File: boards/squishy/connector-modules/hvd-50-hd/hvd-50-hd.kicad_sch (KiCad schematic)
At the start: 14 parts, among them J1 SCSI PHY Mezz, J3 Conn_01x04, J5 HD-50, U1 M24C02-RMC

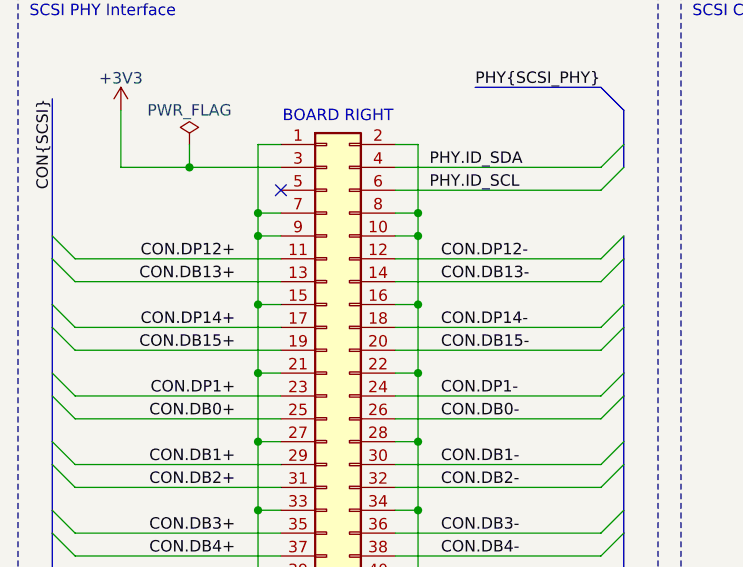
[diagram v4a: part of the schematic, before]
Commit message: squishy: connectors: s/DP12/DB12/g s/DP14/DB14/g
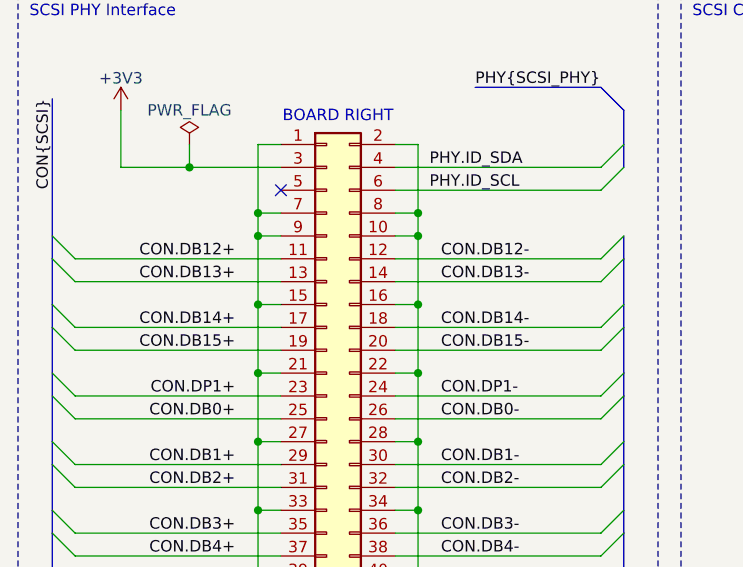
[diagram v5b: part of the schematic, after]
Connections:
- net CON.DP12+ renamed CON.DB12+
- net CON.DP12- renamed CON.DB12-
- net CON.DP14+ renamed CON.DB14+
- net CON.DP14- renamed CON.DB14-
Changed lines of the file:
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@@
 		)
 	)
-	(label "CON.DP14-"
+	(label "CON.DB14-"
 		(at 60.96 52.07 0)
 		(fields_autoplaced yes)
@@
 		)
 	)
-	(label "CON.DP12+"
+	(label "CON.DB12+"
 		(at 38.1 44.45 180)
 		(fields_autoplaced yes)
@@
 		)
 	)
-	(label "CON.DP12-"
+	(label "CON.DB12-"
 		(at 60.96 44.45 0)
 		(fields_autoplaced yes)
@@
 		)
 	)
-	(label "CON.DP14+"
+	(label "CON.DB14+"
 		(at 38.1 52.07 180)
 		(fields_autoplaced yes)

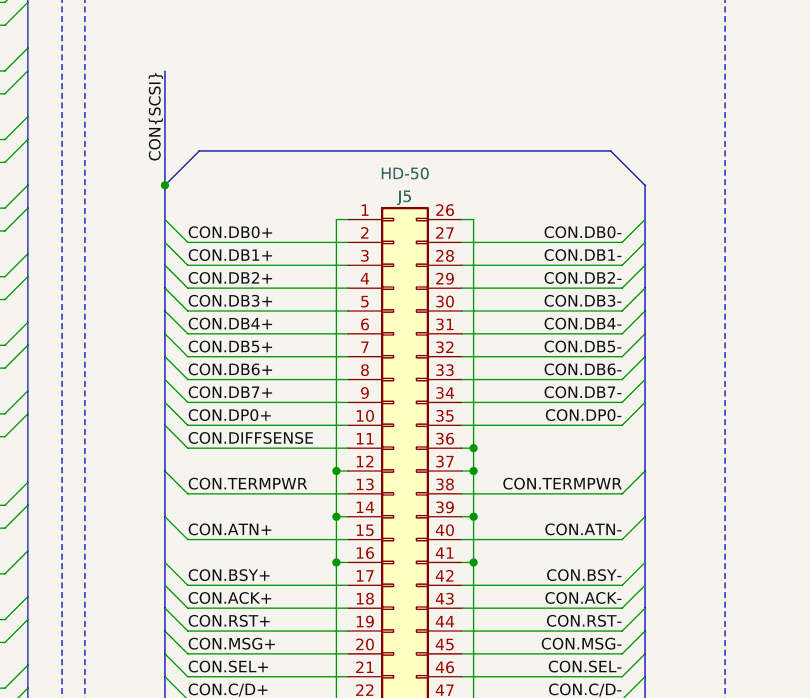
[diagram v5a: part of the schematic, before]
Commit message: squishy: connectors: updated SCSI connector metadata for hvd-50-hd
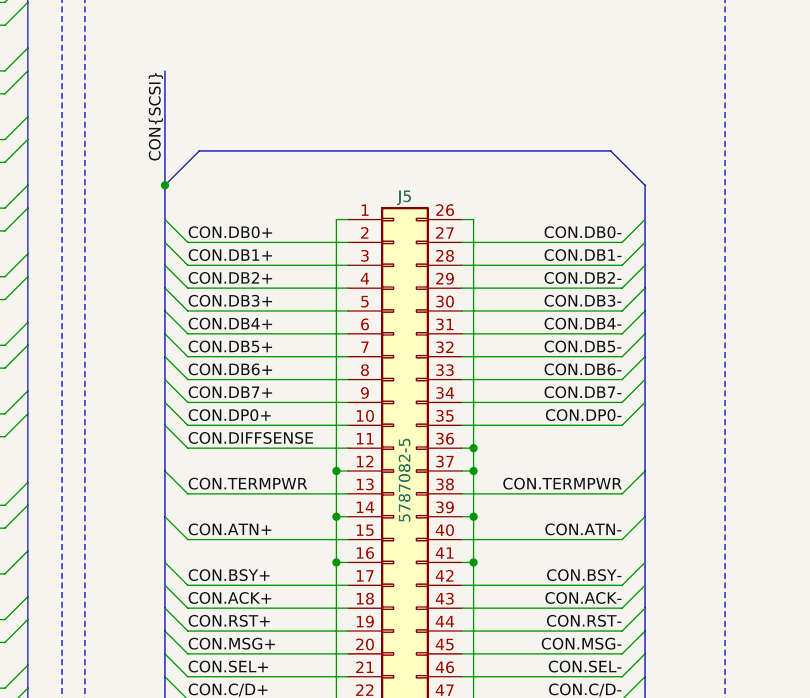
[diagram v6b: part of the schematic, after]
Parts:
- J5: value HD-50 -> 5787082-5; MFR (none) -> TE Connectivity; MPN (none) -> 5787082-5; URL (none) -> https://www.te.com/en/product-5787082-5.html
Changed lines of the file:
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@@
 			)
 		)
-		(property "Value" "HD-50"
-			(at 123.19 63.5 0)
+		(property "Value" "5787082-5"
+			(at 123.19 97.536 90)
 			(effects
 				(font
@@
 			)
 		)
-		(property "Datasheet" "~"
+		(property "Datasheet" "https://www.te.com/commerce/DocumentDelivery/DDEController?Action=showdoc&DocId=Specification+Or+Standard%7F114-40029%7FJ%7Fpdf%7FEnglish%7FENG_SS_114-40029_J.pdf%7F5787082-5"
 			(at 121.92 116.84 0)
 			(effects
@@
 			)
 		)
-		(property "Description" "Generic connector, double row, 02x25, counter clockwise pin numbering scheme (similar to DIP package numbering), with shielding"
+		(property "Description" "AMPLITE 1.27mm High-density D-subminiature 50-pin connector"
 			(at 123.19 97.79 0)
 			(effects
+				(font
+					(size 1.27 1.27)
+				)
+				(hide yes)
+			)
+		)
+		(property "MFR" "TE Connectivity"
+			(at 123.19 97.79 0)
+			(effects
+				(font
+					(size 1.27 1.27)
+				)
+				(hide yes)
+			)
+		)
+		(property "MPN" "5787082-5"
+			(at 123.19 97.79 0)
+			(effects
+				(font
+					(size 1.27 1.27)
+				)
+				(hide yes)
+			)
+		)
+		(property "URL" "https://www.te.com/en/product-5787082-5.html"
+			(at 123.19 97.79 0)
+			(effects

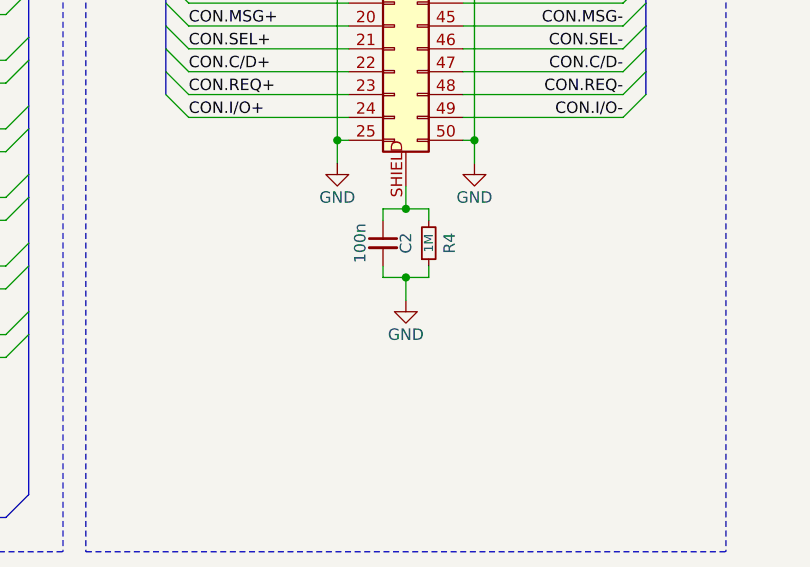
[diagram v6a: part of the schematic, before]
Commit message: squishy: connectors: Routed and length matched the hvd-50-hd connector interface
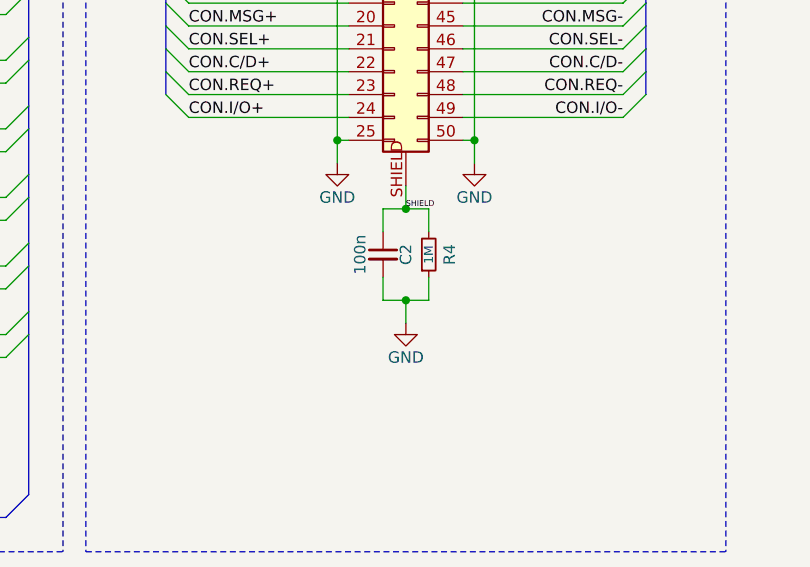
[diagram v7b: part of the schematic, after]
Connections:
- net SHIELD: now reaches C2.1, J5.SHIELD, R4.2
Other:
- moved on the sheet: C2, R4
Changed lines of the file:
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@@
 	)
 	(junction
-		(at 123.19 144.78)
+		(at 123.19 147.32)
 		(diameter 0)
 		(color 0 0 0 0)
@@
 	(wire
 		(pts
-			(xy 123.19 144.78) (xy 125.73 144.78)
+			(xy 123.19 147.32) (xy 125.73 147.32)
 		)
 		(stroke
@@
 	(wire
 		(pts
-			(xy 125.73 137.16) (xy 125.73 138.43)
+			(xy 125.73 137.16) (xy 125.73 139.7)
 		)
 		(stroke
@@
 	(wire
 		(pts
-			(xy 123.19 144.78) (xy 123.19 147.32)
+			(xy 123.19 147.32) (xy 123.19 149.86)
 		)
 		(stroke
@@
 	(wire
 		(pts
-			(xy 120.65 143.51) (xy 120.65 144.78)
+			(xy 120.65 144.78) (xy 120.65 147.32)
+		)
+		(stroke
+			(width 0)
+			(type default)
+		)
+	)
+	(wire
+		(pts
+			(xy 125.73 144.78) (xy 125.73 147.32)
 		)
 		(stroke
@@
 		)
 	)
-	(wire
-		(pts
-			(xy 125.73 143.51) (xy 125.73 144.78)
-		)
-		(stroke
-			(width 0)
-			(type default)
-		)
-	)
 	(bus
 		(pts
@@
 	(wire
 		(pts
-			(xy 120.65 137.16) (xy 120.65 138.43)
+			(xy 120.65 137.16) (xy 120.65 139.7)
 		)
 		(stroke
@@
 	(wire
 		(pts
-			(xy 120.65 144.78) (xy 123.19 144.78)
+			(xy 120.65 147.32) (xy 123.19 147.32)
 		)
 		(stroke
@@
 		)
 	)
+	(label "SHIELD"
+		(at 123.19 137.16 0)
+		(fields_autoplaced yes)
+		(effects
+			(font
+				(size 0.635 0.635)
+			)
+			(justify left bottom)
+		)
+	)
 	(label "CON.I{slash}O+"
 		(at 99.06 127 0)
@@
 	(symbol
 		(lib_id "power:GND")
-		(at 123.19 147.32 0)
+		(at 123.19 149.86 0)
 		(unit 1)
 		(exclude_from_sim no)
@@
 		(dnp no)
 		(property "Reference" "#PWR012"
-			(at 123.19 153.67 0)
+			(at 123.19 156.21 0)
 			(effects
 				(font
@@
 		)
 		(property "Value" "GND"
-			(at 123.19 151.13 0)
+			(at 123.19 153.67 0)
 			(effects
 				(font
@@
 		)
 		(property "Footprint" ""
-			(at 123.19 147.32 0)
+			(at 123.19 149.86 0)
 			(effects
 				(font
@@
 		)
 		(property "Datasheet" ""
-			(at 123.19 147.32 0)
+			(at 123.19 149.86 0)
 			(effects
 				(font
@@
 		)
 		(property "Description" "Power symbol creates a global label with name \"GND\" , ground"
-			(at 123.19 147.32 0)
+			(at 123.19 149.86 0)
 			(effects
 				(font
@@
 	(symbol
 		(lib_id "Device:R_Small")
-		(at 125.73 140.97 0)
+		(at 125.73 142.24 0)
 		(mirror x)
 		(unit 1)
@@
 		(dnp no)
 		(property "Reference" "R4"
-			(at 128.778 140.97 90)
+			(at 128.778 142.24 90)
 			(effects
 				(font
@@
 		)
 		(property "Value" "1M"
-			(at 125.73 140.97 90)
+			(at 125.73 142.24 90)
 			(effects
 				(font
@@
 		)
 		(property "Footprint" "rhais_rcl:R0603"
-			(at 125.73 140.97 0)
+			(at 125.73 142.24 0)
 			(effects
 				(font
@@
 		)
 		(property "Datasheet" ""
-			(at 125.73 140.97 0)
+			(at 125.73 142.24 0)
 			(effects
 				(font
@@
 		)
 		(property "Description" ""
-			(at 125.73 140.97 0)
+			(at 125.73 142.24 0)
 			(effects
 				(font
@@
 		)
 		(property "MFR" ""
-			(at 125.73 140.97 90)
+			(at 125.73 142.24 90)
 			(effects
 				(font
@@
 		)
 		(property "MPN" ""
-			(at 125.73 140.97 90)
+			(at 125.73 142.24 90)
 			(effects
 				(font
@@
 		)
 		(property "Tolerance" ""
-			(at 125.73 140.97 0)
+			(at 125.73 142.24 0)
 			(effects
 				(font
@@
 		)
 		(property "SUPPLIER" "DigiKey"
-			(at 125.73 140.97 0)
+			(at 125.73 142.24 0)
 			(effects
 				(font
@@
 		)
 		(property "SUPPLIER_OC" ""
-			(at 125.73 140.97 0)
+			(at 125.73 142.24 0)
 			(effects
 				(font
@@
 		)
 		(property "SUPPLIER_URL" ""
-			(at 125.73 140.97 0)
+			(at 125.73 142.24 0)
 			(effects
 				(font
@@
 	(symbol
 		(lib_id "Device:C_Small")
-		(at 120.65 140.97 0)
+		(at 120.65 142.24 0)
 		(unit 1)
 		(exclude_from_sim no)
@@
 		(dnp no)
 		(property "Reference" "C2"
-			(at 123.19 140.97 90)
+			(at 123.19 142.24 90)
 			(effects
 				(font
@@
 		)
 		(property "Value" "100n"
-			(at 118.11 140.97 90)
+			(at 118.11 142.24 90)
 			(effects
 				(font
@@
 		)
 		(property "Footprint" "rhais_rcl:C0603"
-			(at 120.65 140.97 0)
+			(at 120.65 142.24 0)
 			(effects
 				(font
@@
 		)
 		(property "Datasheet" "https://content.kemet.com/datasheets/KEM_C1006_X5R_SMD.pdf"
-			(at 120.65 140.97 0)
+			(at 120.65 142.24 0)
 			(effects
 				(font
@@
 		)
 		(property "Description" ""
-			(at 120.65 140.97 0)
+			(at 120.65 142.24 0)
 			(effects
 				(font
@@
 		)
 		(property "MFR" "KEMET"
-			(at 120.65 140.97 90)
+			(at 120.65 142.24 90)
 			(effects
 				(font
@@
 		)
 		(property "MPN" "C0603C104M5RACTU"
-			(at 120.65 140.97 90)
+			(at 120.65 142.24 90)
 			(effects
 				(font
@@
 		)
 		(property "Tolerance" "±20% 50V"
-			(at 120.65 140.97 0)
+			(at 120.65 142.24 0)
 			(effects
 				(font
@@
 		)
 		(property "SUPPLIER" "DigiKey"
-			(at 120.65 140.97 0)
+			(at 120.65 142.24 0)
 			(effects
 				(font
@@
 		)
 		(property "SUPPLIER_OC" "399-C0603C104M5RAC7867DKR-ND"
-			(at 120.65 140.97 0)
+			(at 120.65 142.24 0)
 			(effects
 				(font
@@
 		)
 		(property "SUPPLIER_URL" "https://www.digikey.com/short/8nqzrr4b"
-			(at 120.65 140.97 0)
+			(at 120.65 142.24 0)
 			(effects
 				(font

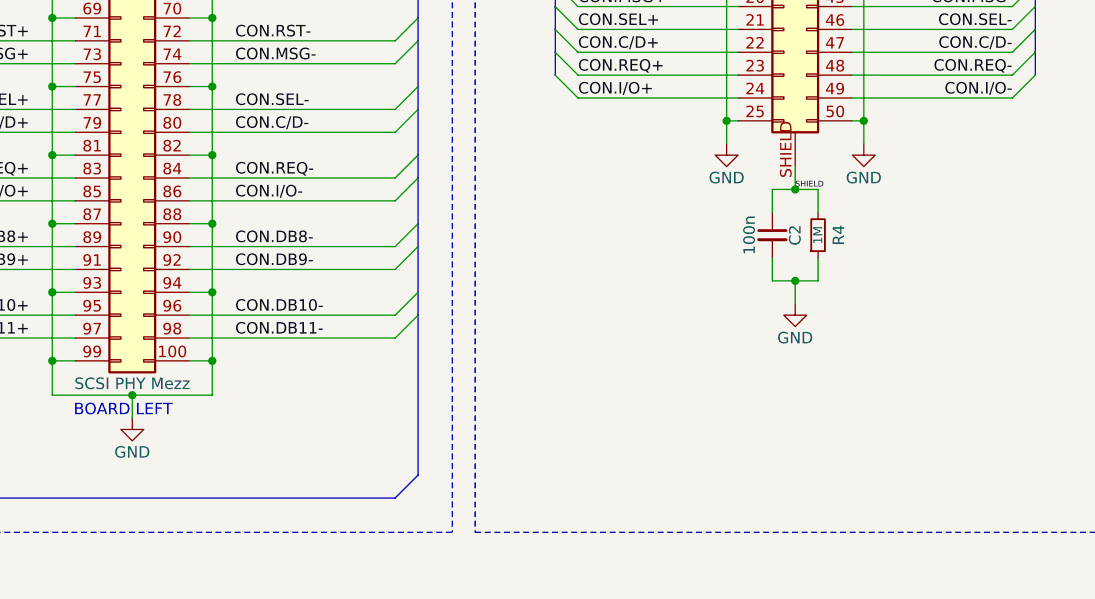
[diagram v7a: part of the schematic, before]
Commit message: squishy: connectors: Adjustments for ERC and DRC cleanliness for hvd-50-hd connector interface board
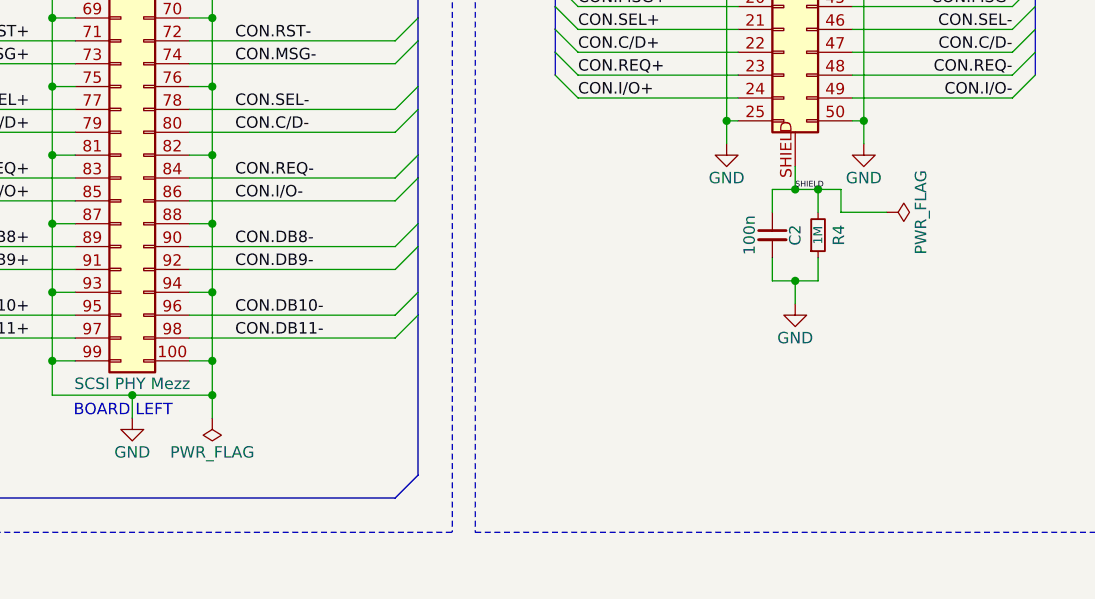
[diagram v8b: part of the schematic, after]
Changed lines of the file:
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@@
 	)
 	(junction
+		(at 125.73 137.16)
+		(diameter 0)
+		(color 0 0 0 0)
+	)
+	(junction
 		(at 123.19 137.16)
 		(diameter 0)
@@
 	)
 	(junction
+		(at 58.42 160.02)
+		(diameter 0)
+		(color 0 0 0 0)
+	)
+	(junction
 		(at 58.42 156.21)
 		(diameter 0)
@@
 	(wire
 		(pts
+			(xy 128.27 137.16) (xy 128.27 139.7)
+		)
+		(stroke
+			(width 0)
+			(type default)
+		)
+	)
+	(wire
+		(pts
 			(xy 78.74 113.03) (xy 55.88 113.03)
 		)
@@
 	(wire
 		(pts
+			(xy 128.27 139.7) (xy 133.35 139.7)
+		)
+		(stroke
+			(width 0)
+			(type default)
+		)
+	)
+	(wire
+		(pts
 			(xy 129.54 101.6) (xy 130.81 101.6)
 		)
@@
 		)
 	)
+	(wire
+		(pts
+			(xy 125.73 137.16) (xy 128.27 137.16)
+		)
+		(stroke
+			(width 0)
+			(type default)
+		)
+	)
 	(bus
 		(pts
@@
 	(wire
 		(pts
+			(xy 58.42 162.56) (xy 58.42 160.02)
+		)
+		(stroke
+			(width 0)
+			(type default)
+		)
+	)
+	(wire
+		(pts
 			(xy 99.06 88.9) (xy 116.84 88.9)
 		)
@@
 	)
 	(symbol
+		(lib_id "power:PWR_FLAG")
+		(at 133.35 139.7 270)
+		(unit 1)
+		(exclude_from_sim no)
+		(in_bom yes)
+		(on_board yes)
+		(dnp no)
+		(property "Reference" "#FLG03"
+			(at 135.255 139.7 0)
+			(effects
+				(font
+					(size 1.27 1.27)
+				)
+				(hide yes)
+			)
+		)
+		(property "Value" "PWR_FLAG"
+			(at 137.16 139.7 0)
+			(effects
+				(font
+					(size 1.27 1.27)
+				)
+			)
+		)
+		(property "Footprint" ""
+			(at 133.35 139.7 0)
+			(effects
+				(font
+					(size 1.27 1.27)
+				)
+				(hide yes)
+			)
+		)
+		(property "Datasheet" "~"
+			(at 133.35 139.7 0)
+			(effects
+				(font
+					(size 1.27 1.27)
+				)
+				(hide yes)
+			)
+		)
+		(property "Description" "Special symbol for telling ERC where power comes from"
+			(at 133.35 139.7 0)
+			(effects
+				(font
+					(size 1.27 1.27)
+				)
+				(hide yes)
+			)
+		)
+		(pin "1"
+		)
+		(instances
+			(project "hvd-50-hd"
+				(path "/bd9eafec-5355-49e4-b2e3-916daacb0a86"
+					(reference "#FLG03")
+					(unit 1)
+				)
+			)
+		)
+	)
+	(symbol
 		(lib_id "Mechanical:MountingHole_Pad")
 		(at 187.96 144.78 0)
@@
 					(unit 1)
 				)
+			)
+		)
+	)
+	(symbol
+		(lib_id "power:PWR_FLAG")
+		(at 58.42 162.56 180)
+		(unit 1)
+		(exclude_from_sim no)
+		(in_bom yes)
+		(on_board yes)
+		(dnp no)
+		(property "Reference" "#FLG02"
+			(at 58.42 164.465 0)
+			(effects
+				(font
+					(size 1.27 1.27)
+				)
+				(hide yes)
+			)
+		)
+		(property "Value" "PWR_FLAG"
+			(at 58.42 166.37 0)
+			(effects
+				(font
+					(size 1.27 1.27)
+				)
+			)
+		)
+		(property "Footprint" ""
+			(at 58.42 162.56 0)
+			(effects
+				(font
+					(size 1.27 1.27)
+				)
+				(hide yes)
+			)
+		)
+		(property "Datasheet" "~"
+			(at 58.42 162.56 0)
+			(effects
+				(font
+					(size 1.27 1.27)
+				)
+				(hide yes)
+			)
+		)
+		(property "Description" "Special symbol for telling ERC where power comes from"
+			(at 58.42 162.56 0)
+			(effects
+				(font
+					(size 1.27 1.27)
+				)
+				(hide yes)
+			)
+		)
+		(pin "1"
+		)
+		(instances
+			(project "hvd-50-hd"
+				(path "/bd9eafec-5355-49e4-b2e3-916daacb0a86"
+					(reference "#FLG02")
+					(unit 1)
+				)
